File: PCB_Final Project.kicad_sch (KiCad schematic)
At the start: 25 parts, among them J1 Conn_01x02_Socket, J2 Conn_01x02_Pin, J3 Conn_01x02_Socket, K1 Relay_SPDT, Q1 NPN, U1 WeMos_D1_mini, U2 PC817

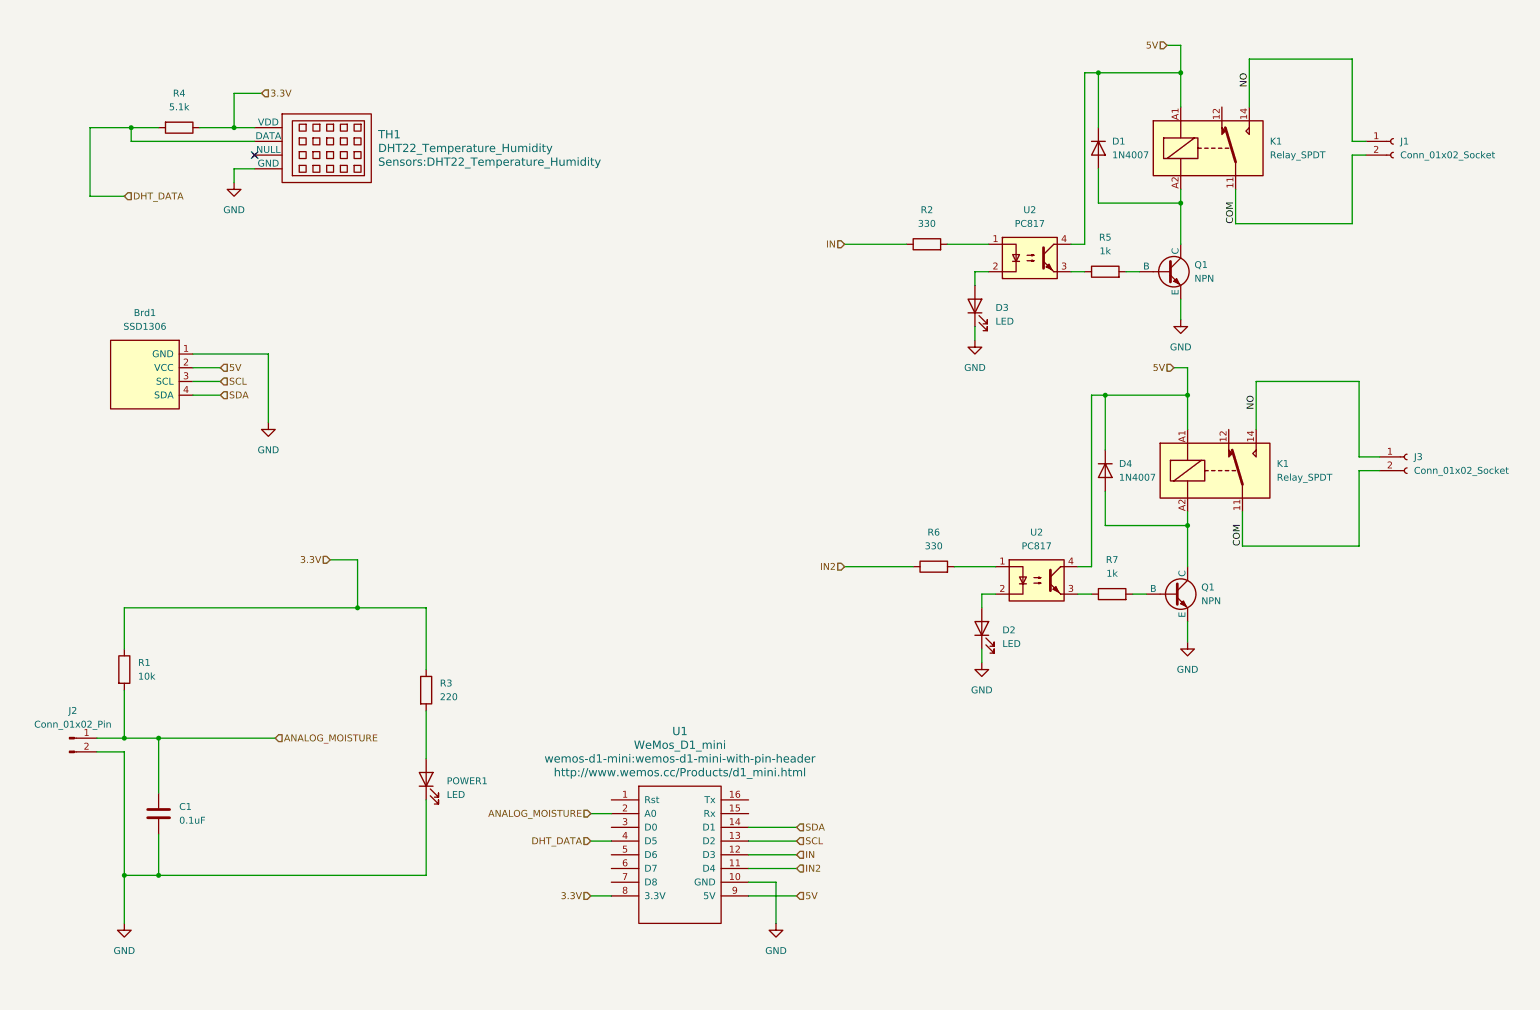
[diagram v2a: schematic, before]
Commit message: add alternate power & revamp pcb
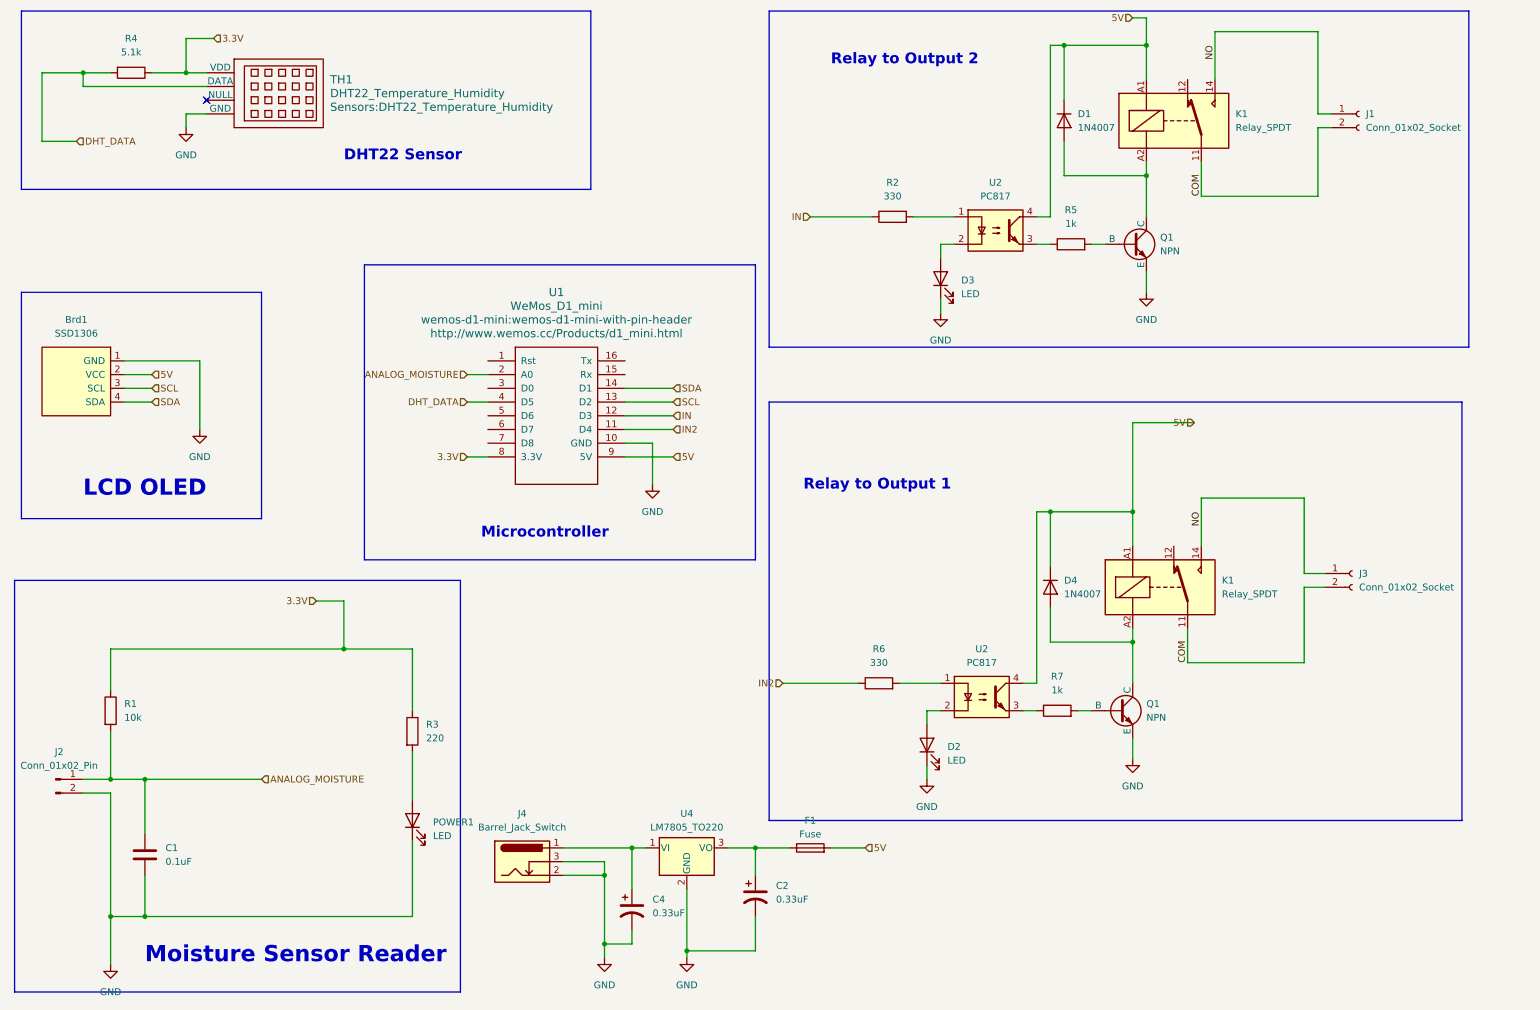
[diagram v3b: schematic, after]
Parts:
- added C2, C4: 0.33uF, Capacitor_SMD:C_0805_2012Metric, symbol Device:C_Polarized_US
- added F1: Fuse, Fuse:Fuse_0805_2012Metric, symbol Device:Fuse
- added J4: Barrel_Jack_Switch, Connector_BarrelJack:BarrelJack_Horizontal, symbol Connector:Barrel_Jack_Switch
- added U4: LM7805_TO220, Package_TO_SOT_THT:TO-220-3_Vertical, symbol Regulator_Linear:LM7805_TO220
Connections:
- net 5V: now also F1.2
- net GND: now also C2.2, C4.2, J4.2, J4.3, U4.2 (GND)
- new net: C4.1, J4.1, U4.1 (VI)
- new net: C2.1, F1.1, U4.3 (VO)
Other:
- note added: "DHT22 Sensor"
- note added: "LCD OLED"
- note added: "Microcontroller"
- note added: "Moisture Sensor Reader"
- note added: "Relay to Output 1"
- note added: "Relay to Output 2"
- moved on the sheet: Brd1, C1, D1, D2, D3, D4, J1, J2, J3, K1, POWER1, Q1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

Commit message: final commit
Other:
- note added: "Alternate Power & Protection"
- note added: "Relay Output"
- note removed: "Relay to Output 1"
- note removed: "Relay to Output 2"
- title: (none) -> GreenConnect
- moved on the sheet: Brd1, C2, C4, D2, D4, F1, J3, J4, K1, POWER1, Q1, R3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
